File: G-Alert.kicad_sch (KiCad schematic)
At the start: 15 parts, among them Q1 BT169D, SW2 SW_Push_Open, U1 MQ-6, U2 LM393

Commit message: Prototype Update
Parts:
- removed Q1: BT169D, Package_TO_SOT_THT:TO-92_Inline, symbol Triac_Thyristor:BT169D
- removed SW2: SW_Push_Open, symbol Switch:SW_Push_Open
- added D3: NEC24PM, Package_TO_SOT_THT:TO-126-3_Vertical, symbol Device:Q_SCR_KAG
- added P1: USB_C_Plug_USB2.0, symbol Connector:USB_C_Plug_USB2.0
- added SW1: SW_Push, symbol Switch:SW_Push
- U1: value MQ-6 -> MQ-4b
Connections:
- net +5V: now also BZ1.1 (+), R6.1, P1.A4 (VBUS), P1.A9 (VBUS), P1.B4 (VBUS), P1.B9 (VBUS)
- net GND: now also D3.1 (K), P1.A1 (GND), P1.A12 (GND), P1.B1 (GND), P1.B12 (GND), SW1.2
- net at BZ1.2 (-), R6.2: now also D3.2 (A), SW1.1
- net at C1.2, D1.1 (K), R2.1: now also D3.3 (G)
- no-connect marks 0 -> 5
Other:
- moved on the sheet: BZ1, C1, D1, D2, R1, R2, R3, R4, R5, R6, R_Var, U1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

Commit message: Final Update on Schematics
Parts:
- added D4: D, symbol Device:D
- C1: value 0.1uF -> 10uF
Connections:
- net at D3.3 (G), R2.1: now also D4.1 (K); no longer C1.2, D1.1 (K)
- new net: C1.2, D1.1 (K), D4.2 (A)
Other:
- moved on the sheet: BZ1, D1, D2, D3, P1, R1, R2, R3, R4, R5, R6, R_Var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

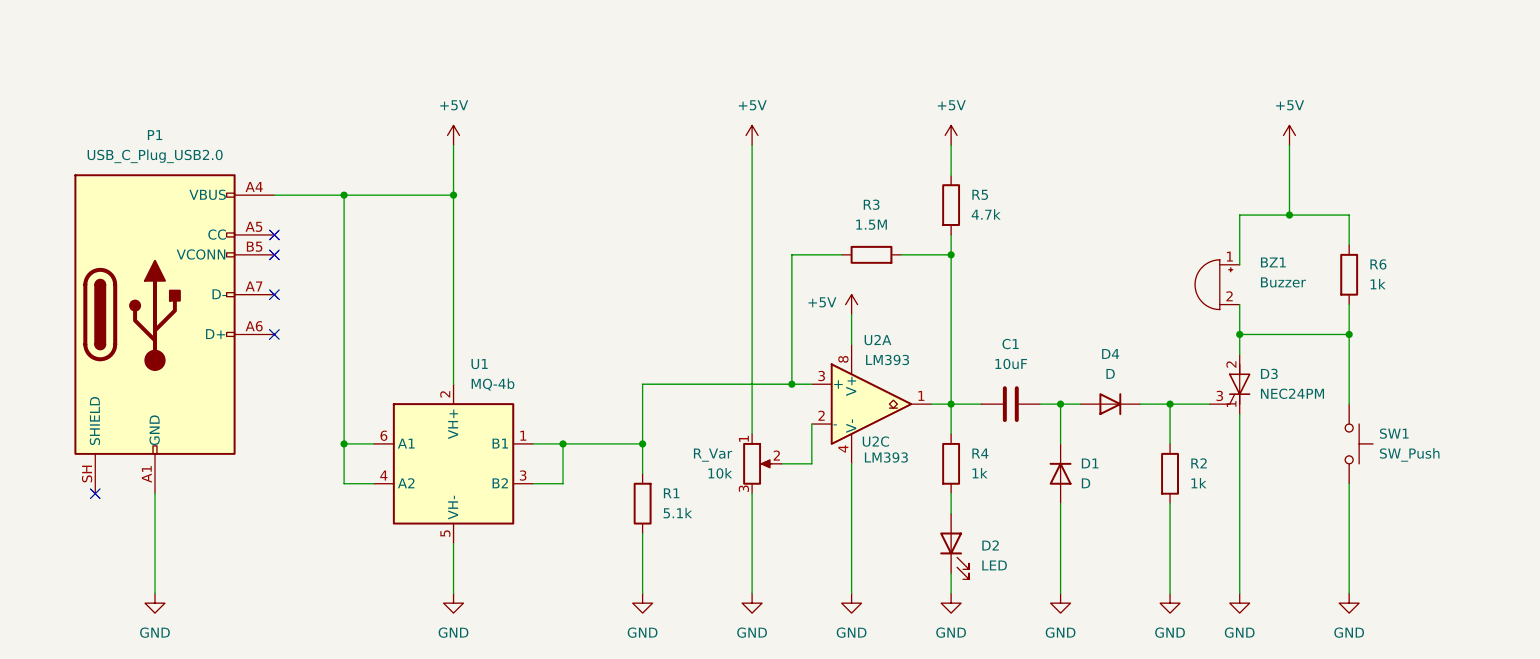
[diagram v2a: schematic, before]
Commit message: Footprint Update
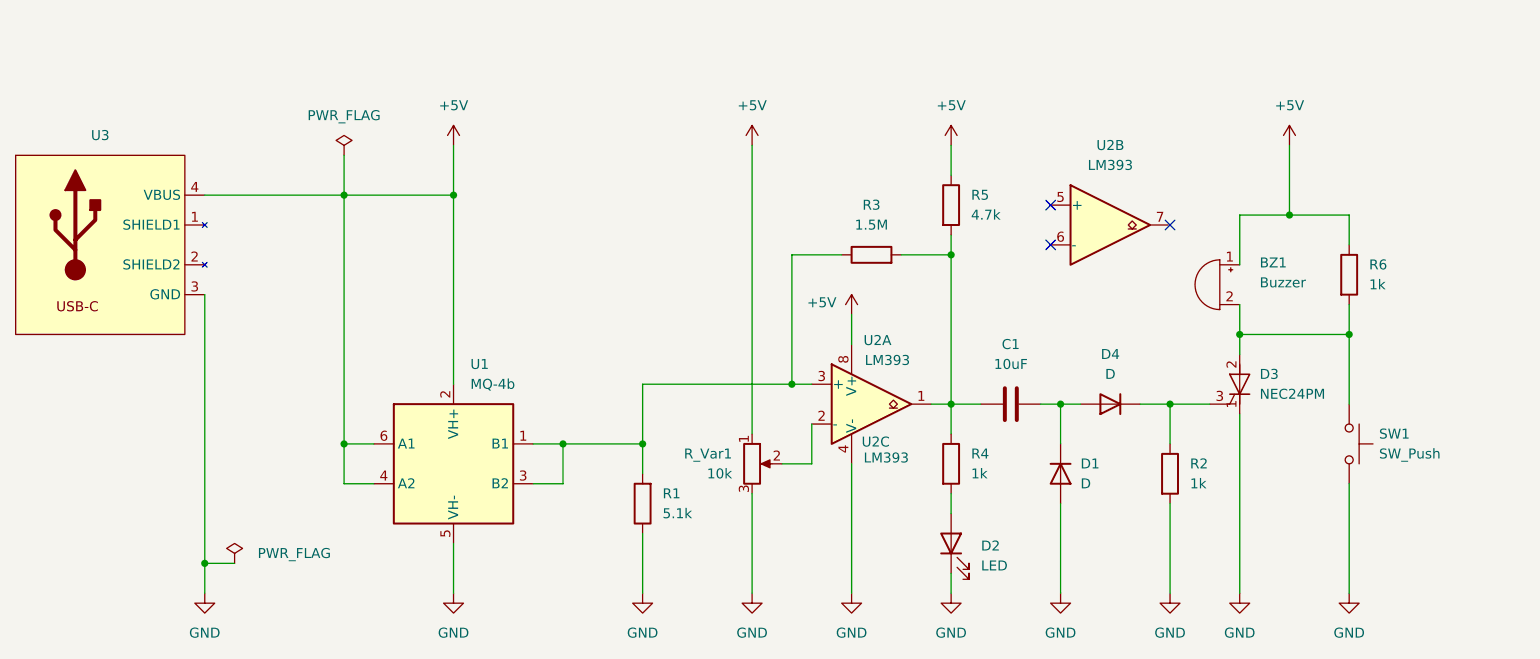
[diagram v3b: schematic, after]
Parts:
- removed P1: USB_C_Plug_USB2.0, symbol Connector:USB_C_Plug_USB2.0
- added unit 2 of U2
- added U3: (no value), USB-C Connector:USB-C, symbol USB-C Connector:USB-C
- BZ1: footprint (none) -> Buzzer_Beeper:Buzzer_12x9.5RM7.6
- C1: footprint (none) -> Capacitor_THT:CP_Radial_D5.0mm_P2.00mm
- D1, D4: footprint (none) -> Diode_THT:D_DO-35_SOD27_P7.62mm_Horizontal
- D2: footprint (none) -> LED_THT:LED_D5.0mm
- R1, R2, R3, R4, R5, R6: footprint (none) -> Resistor_THT:R_Axial_DIN0207_L6.3mm_D2.5mm_P10.16mm_Horizontal
- R_Var1: renamed from R_Var; footprint (none) -> Potentiometer_THT:Potentiometer_Piher_PT-10-V05_Vertical
- SW1: footprint (none) -> Button_Switch_THT:SW_PUSH_6mm
- U2: footprint (none) -> Package_DIP:DIP-8_W7.62mm
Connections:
- net +5V: now also U3.4 (VBUS)
- net GND: now also U3.3 (GND)
- no-connect marks 5 -> 3

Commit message: LED Update
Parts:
- added D5: LED, LED_THT:LED_D5.0mm, symbol Device:LED
- added R7: 1k, Resistor_THT:R_Axial_DIN0207_L6.3mm_D2.5mm_P10.16mm_Horizontal, symbol Device:R
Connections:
- net +5V: now also R7.1
- net GND: now also D5.1 (K)
- new net: D5.2 (A), R7.2

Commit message: Panel Update
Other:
- company: (none) -> Bivob.BD
- title: G-Alert -> G-Alert Schematics
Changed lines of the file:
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@@
 	(paper "A4")
 	(title_block
-		(title "G-Alert")
+		(title "G-Alert Schematics")
+		(company "Bivob.BD")
 	)
 	(junction
